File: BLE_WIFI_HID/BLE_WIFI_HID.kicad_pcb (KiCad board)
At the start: 2 copper layers, 63.3 x 34 mm, 22 parts, among them P1 CONN_01X07, P2 CONN_01X07, P3 PROGRAMMER SERIAL, P4 Battery, SW1 SW_Push, U1 ESP32-WROOM, U2 AP2112K-3.3TRG1, U3 MCP73831T-2ACI/OT

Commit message: clean and new position
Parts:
- moved R6 5.18 mm to (178.0, 85.0)
- moved C4 4.67 mm to (184.2, 91.3)
- moved U3 4.04 mm to (178.2, 90.0)
- moved P4 3.88 mm to (183.0, 85.9)
- moved R3 3.80 mm to (152.8, 84.9), turned to 90 degrees
- moved P3 3.76 mm to (136.5, 84.4)
- moved C3 2.31 mm to (174.1, 99.9)
- moved D2 2.24 mm to (177.6, 99.8)
- moved SW1 2.00 mm to (168.5, 102.0)
- moved D1 1.88 mm to (156.8, 83.5)
- moved R7 1.86 mm to (169.9, 88.3)
- moved C2 1.74 mm to (181.7, 104.9)
- moved D3 1.65 mm to (173.2, 88.3)
- moved U2 1.40 mm to (182.2, 100.4)
- moved R5 1.13 mm to (181.6, 107.8)
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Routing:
- net VCC: track 126.3 -> 183.3 mm
- net GND: track 176.0 -> 197.0 mm
- net /IO0_BOOT/DTR: track 25.5 -> 15.9 mm
- net /TX_ESP32: track 42.6 -> 33.0 mm
- net /IO13: track 13.1 -> 6.50 mm
- net /RX_ESP32: track 36.2 -> 30.9 mm
- net +3V3: track 35.6 -> 30.3 mm
- net Net-(R7-Pad1): track 12.6 -> 7.97 mm
- net Net-(R7-Pad2): track 9.25 -> 13.3 mm
- net /RESET/RTS: track 56.1 -> 52.1 mm
- net Net-(D3-Pad1): track 2.14 -> 5.33 mm
- net Net-(D3-Pad2): track 2.83 -> 5.06 mm
- net +BATT: track 30.2 -> 28.4 mm
- added copper zone on F.Cu, net GND
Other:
- board size 63.3 x 34 mm -> 62.9 x 33.4 mm

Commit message: change the connectors
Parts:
- P1, P2: moved to B.Cu
- turned P1 to 0 degrees
- turned P2 to 180 degrees

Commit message: Auto stash before merge of "master" and "origin/master"
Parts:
- moved C3 68.7 mm to (120.5, 56.9)
- moved C1 68.7 mm to (115.1, 63.0)
- moved C2 68.7 mm to (128.1, 61.9)
- moved C4 68.7 mm to (130.6, 48.4)
- moved D1 68.7 mm to (103.2, 40.5)
- moved D2 68.7 mm to (124.0, 56.8)
- moved D3 68.7 mm to (119.7, 45.4)
- moved P3 68.7 mm to (82.9, 41.4)
- moved P4 68.7 mm to (129.4, 42.9)
- moved R1 68.7 mm to (116.2, 50.9)
- moved R2 68.7 mm to (113.6, 50.9)
- moved R3 68.7 mm to (99.3, 41.9)
- moved R4 68.7 mm to (114.6, 55.6)
- moved R5 68.7 mm to (128.1, 64.8)
- moved R6 68.7 mm to (124.4, 42.0)
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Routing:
- net GND: track 197.0 -> 202.6 mm
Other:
- outline, holes or cut-outs redrawn

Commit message: update to v0.3 pcb
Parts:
- removed P1, P2: CONN_01X07, Pin_Headers:Pin_Header_Straight_1x07_Pitch2.54mm
- removed SW1: SW_Push, TIH:SW_B3U-1000P
- added G***: LOGO, Aesthetics:electronic_cats_logo_8x6, B.Cu at (111.7, 49.4)
- added G***: LOGO, Aesthetics:meowmeow_logo_21x8, B.Cu at (113.5, 38.9)
- added G***: LOGO, Aesthetics:beta_testing, F.Cu at (83.4, 64.2)
- added J1: Conn_02x03_Odd_Even, Pines:62000621121, F.Cu at (136.4, 53.7)
- added J2: Conn_02x03_Odd_Even, Pines:62000621121, F.Cu at (80.8, 53.5)
- added R8: 10K, Resistors_SMD:R_0805_HandSoldering, F.Cu at (120.0, 65.3)
- R4: value 1k -> 10k
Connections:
- net /IO0_BOOT/DTR renamed /ESP_GPIO0
- net /RX_ESP32 renamed /ESP_RX
- net /TX_ESP32 renamed /ESP_TX
- P3 pad 5: /RESET/RTS -> /ESP_RESET
- R3 pad 1: /IO13 -> /IO25
- R4 pad 1: +3V3 -> /ESP_RESET
- R4 pad 2: /RESET/RTS -> GND
- U1 pad 10: Net-(U1-Pad10) -> /IO25
- U1 pad 13: Net-(U1-Pad13) -> /MOSI
- U1 pad 16: /IO13 -> Net-(U1-Pad16)
- U1 pad 29: Net-(U1-Pad29) -> /ESP_CS
- U1 pad 3: /RESET/RTS -> /ESP_RESET
- U1 pad 30: Net-(U1-Pad30) -> /SCK
- U1 pad 31: Net-(U1-Pad31) -> /ESP_RTS
- U1 pad 37: Net-(U1-Pad37) -> /MISO
- U1 pad 7: /AN35_BAT -> Net-(U1-Pad7)
- U1 pad 9: Net-(U1-Pad9) -> /ESP_BUSY
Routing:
- net GND: track 202.6 -> 0.00 mm
- net VCC: track 183.4 -> 0.00 mm
- net /RESET/RTS: track 52.1 -> 0.00 mm
- net /ESP_TX: track 32.9 -> 0.00 mm
- net /ESP_RX: track 30.9 -> 0.00 mm
- net +3V3: track 30.3 -> 0.00 mm
- net +BATT: track 28.4 -> 0.00 mm
- net /ESP_GPIO0: track 15.9 -> 0.00 mm
- net /AN35_BAT: track 14.3 -> 0.00 mm
- net Net-(R7-Pad2): track 13.3 -> 0.00 mm
- net Net-(R7-Pad1): track 7.97 -> 0.00 mm
- net Net-(R5-Pad1): track 7.97 -> 0.00 mm
- net /IO13: track 6.50 -> 0.00 mm
- net Net-(D3-Pad1): track 5.33 -> 0.00 mm
- net Net-(D3-Pad2): track 5.06 -> 0.00 mm
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
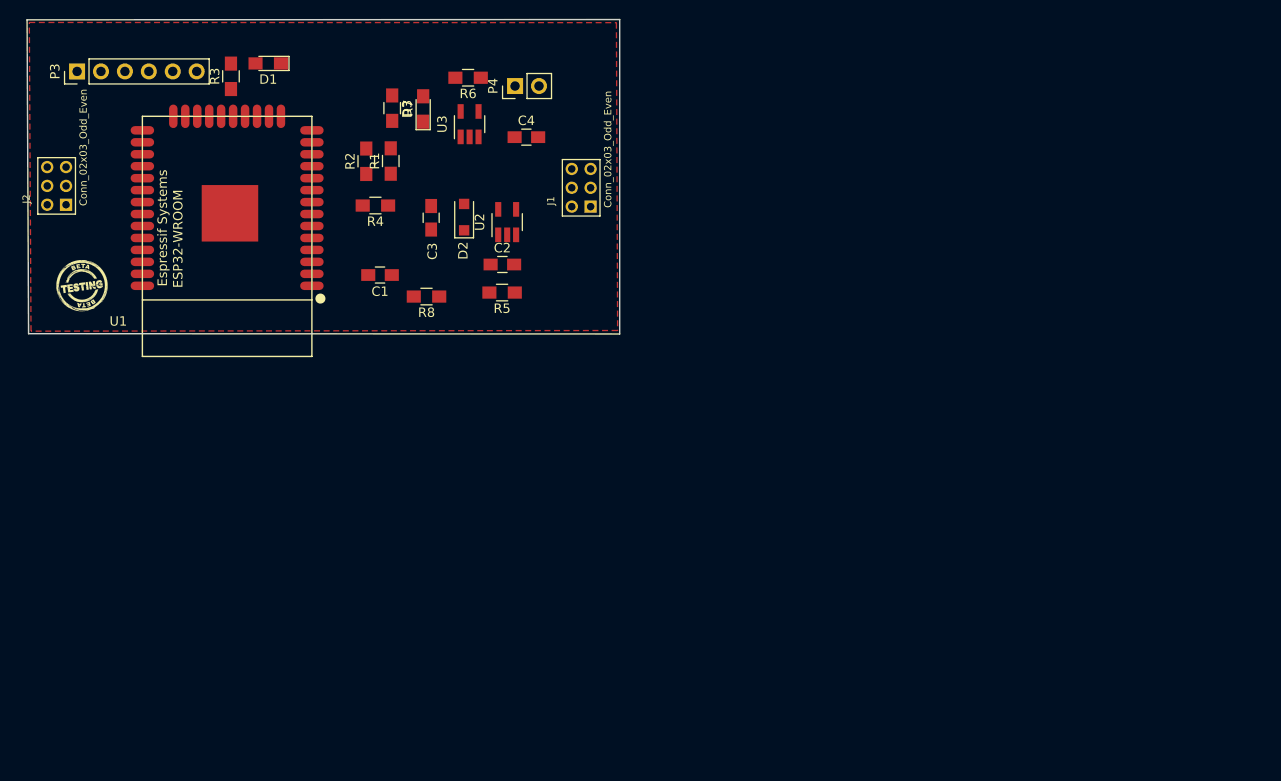
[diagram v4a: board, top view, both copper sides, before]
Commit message: update reset resistor ESP32
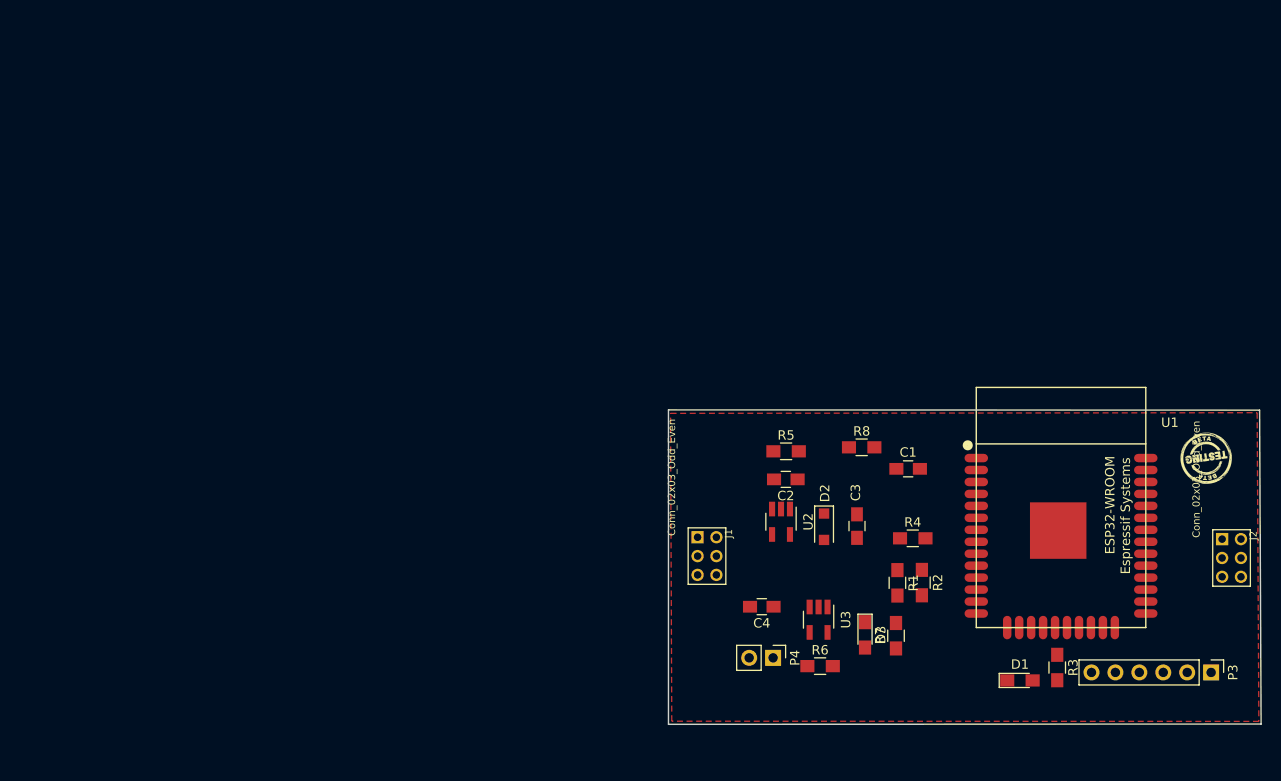
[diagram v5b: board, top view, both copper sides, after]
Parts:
- moved P3 136.3 mm to (203.3, 105.2), turned to 270 degrees
- moved J2 130.9 mm to (205.5, 93.0), turned to 270 degrees
- moved G*** 120.8 mm to (202.8, 82.3), turned to 180 degrees
- moved R3 107.9 mm to (187.0, 104.7), turned to 270 degrees
- moved D1 103.3 mm to (183.0, 106.0), turned to 0 degrees
- moved U1 93.1 mm to (187.4, 87.7), turned to 180 degrees
- moved G*** 92.9 mm to (195.7, 89.0)
- moved G*** 92.1 mm to (195.7, 80.4)
- moved R7 77.5 mm to (169.9, 101.3), turned to 90 degrees
- moved R2 74.0 mm to (172.6, 95.6), turned to 270 degrees
- moved D3 72.9 mm to (166.6, 101.2), turned to 270 degrees
- moved R6 72.8 mm to (161.8, 104.5), turned to 0 degrees
- moved R1 70.0 mm to (170.0, 95.7), turned to 270 degrees
- moved R4 67.1 mm to (171.7, 90.9), turned to 0 degrees
- moved P4 66.6 mm to (156.8, 103.6), turned to 270 degrees
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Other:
- outline, holes or cut-outs redrawn
- board text added: "Backpack BLE"

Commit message: Inicio routeo
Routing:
- net /ESP_GPIO0: track 0.00 -> 89.1 mm
- net /MOSI: track 0.00 -> 61.6 mm
- net /ESP_CS: track 0.00 -> 51.7 mm
- net +BATT: track 0.00 -> 25.8 mm
- net Net-(R7-Pad1): track 0.00 -> 13.4 mm
- net /ESP_RESET: track 0.00 -> 13.1 mm
- net Net-(R7-Pad2): track 0.00 -> 11.9 mm
- net +3V3: track 0.00 -> 11.5 mm
- net Net-(D3-Pad2): track 0.00 -> 5.18 mm
- net /AN35_BAT: track 0.00 -> 5.03 mm
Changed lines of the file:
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@@
-(kicad_pcb (version 20171130) (host pcbnew "(5.0.1-3-g963ef8bb5)")
+(kicad_pcb (version 20171130) (host pcbnew "(5.1.2)-2")
   (general
     (thickness 1.6)
     (drawings 5)
-    (tracks 1)
+    (tracks 83)
     (zones 0)
     (modules 25)
@@
     (zone_45_only no)
     (trace_min 0.2)
-    (segment_width 0.2)
-    (edge_width 0.15)
     (via_size 0.6)
     (via_drill 0.4)
@@
     (uvia_min_size 0.2)
     (uvia_min_drill 0.1)
+    (edge_width 0.15)
+    (segment_width 0.2)
     (pcb_text_width 0.3)
     (pcb_text_size 1.5 1.5)
@@
   (gr_line (start 208.648 110.668) (end 145.718 110.698) (layer Edge.Cuts) (width 0.15))
   (gr_line (start 208.488 77.338) (end 208.648 110.668) (layer Edge.Cuts) (width 0.15))
+  (segment (start 175.6 85.45) (end 170.2 85.45) (width 0.3) (layer F.Cu) (net 1))
+  (segment (start 169.918 85.168) (end 169.918 83.568) (width 0.3) (layer F.Cu) (net 1))
+  (segment (start 170.2 85.45) (end 169.918 85.168) (width 0.3) (layer F.Cu) (net 1))
+  (segment (start 175.95 84.075) (end 175.95 85.1) (width 0.3) (layer F.Cu) (net 1))
+  (segment (start 176.332 83.693) (end 175.95 84.075) (width 0.3) (layer F.Cu) (net 1))
+  (segment (start 178.403 83.693) (end 176.332 83.693) (width 0.3) (layer F.Cu) (net 1))
+  (segment (start 175.95 85.1) (end 175.6 85.45) (width 0.3) (layer F.Cu) (net 1))
+  (segment (start 160.678 98.208) (end 160.708 98.238) (width 0.3) (layer F.Cu) (net 4))
+  (segment (start 156.878 98.208) (end 160.678 98.208) (width 0.3) (layer F.Cu) (net 4))
+  (segment (start 156.828 98.258) (end 156.878 98.208) (width 0.3) (layer F.Cu) (net 4))
+  (segment (start 156.828 103.638) (end 156.828 98.258) (width 0.3) (layer F.Cu) (net 4))
+  (segment (start 162.238 94.038) (end 162.238 91.118) (width 0.3) (layer F.Cu) (net 4))
+  (segment (start 160.708 98.238) (end 160.708 95.917) (width 0.3) (layer F.Cu) (net 4))
+  (segment (start 162.523 94.323) (end 162.4125 94.2125) (width 0.3) (layer F.Cu) (net 4))
+  (segment (start 162.4125 94.2125) (end 162.238 94.038) (width 0.3) (layer F.Cu) (net 4))
+  (segment (start 162.2375 94.0385) (end 162.238 94.038) (width 0.3) (layer F.Cu) (net 4))
+  (segment (start 162.2375 94.3875) (end 162.2375 94.0385) (width 0.3) (layer F.Cu) (net 4))
+  (segment (start 162.2375 94.3875) (end 162.4125 94.2125) (width 0.3) (layer F.Cu) (net 4))
+  (segment (start 162.302 94.323) (end 162.15 94.475) (width 0.3) (layer F.Cu) (net 4))
+  (segment (start 162.727 94.323) (end 162.302 94.323) (width 0.3) (layer F.Cu) (net 4))
+  (segment (start 162.15 94.475) (end 162.2375 94.3875) (width 0.3) (layer F.Cu) (net 4))
+  (segment (start 160.708 95.917) (end 162.15 94.475) (width 0.3) (layer F.Cu) (net 4))
+  (segment (start 170.028 94.323) (end 162.727 94.323) (width 0.3) (layer F.Cu) (net 4))
+  (segment (start 162.727 94.323) (end 162.523 94.323) (width 0.3) (layer F.Cu) (net 4))
   (segment (start 184.408 106.018) (end 184.388 106.038) (width 0.3) (layer F.Cu) (net 5))
+  (segment (start 163.168 104.518) (end 166.232 104.518) (width 0.3) (layer F.Cu) (net 7))
+  (segment (start 166.588 104.162) (end 166.588 102.548) (width 0.3) (layer F.Cu) (net 7))
+  (segment (start 166.232 104.518) (end 166.588 104.162) (width 0.3) (layer F.Cu) (net 7))
+  (segment (start 178.403 97.663) (end 176.162 97.663) (width 0.3) (layer F.Cu) (net 8))
+  (segment (start 176.162 97.663) (end 175.2 98.625) (width 0.3) (layer F.Cu) (net 8))
+  (segment (start 175.2 98.625) (end 175.2 107.9) (width 0.3) (layer F.Cu) (net 8))
+  (segment (start 175.2 107.9) (end 174.675 108.425) (width 0.3) (layer F.Cu) (net 8))
+  (segment (start 174.675 108.425) (end 153.225 108.425) (width 0.3) (layer F.Cu) (net 8))
+  (segment (start 153.225 108.425) (end 152.525 107.725) (width 0.3) (layer F.Cu) (net 8))
+  (segment (start 152.525 107.725) (end 152.525 88.925) (width 0.3) (layer F.Cu) (net 8))
+  (segment (start 152.525 88.925) (end 151.625 88.025) (width 0.3) (layer F.Cu) (net 8))
+  (segment (start 151.625 88.025) (end 149.025 88.025) (width 0.3) (layer F.Cu) (net 8))
+  (segment (start 148.808 88.242) (end 148.808 90.833) (width 0.3) (layer F.Cu) (net 8))
+  (segment (start 149.025 88.025) (end 148.808 88.242) (width 0.3) (layer F.Cu) (net 8))
+  (segment (start 171.678 94.298) (end 171.4 94.576) (width 0.3) (layer F.Cu) (net 11))
+  (segment (start 172.628 94.298) (end 171.678 94.298) (width 0.3) (layer F.Cu) (net 11))
+  (segment (start 171.4 94.576) (end 171.4 96.8) (width 0.3) (layer F.Cu) (net 11))
+  (segment (start 171.177 97.023) (end 170.028 97.023) (width 0.3) (layer F.Cu) (net 11))
+  (segment (start 171.4 96.8) (end 171.177 97.023) (width 0.3) (layer F.Cu) (net 11))
+  (segment (start 168.928 102.638) (end 168 101.71) (width 0.3) (layer F.Cu) (net 13))
+  (segment (start 169.878 102.638) (end 168.928 102.638) (width 0.3) (layer F.Cu) (net 13))
+  (segment (start 168 101.71) (end 168 98.575) (width 0.3) (layer F.Cu) (net 13))
+  (segment (start 168 98.575) (end 167.425 98) (width 0.3) (layer F.Cu) (net 13))
+  (segment (start 167.425 98) (end 165.25 98) (width 0.3) (layer F.Cu) (net 13))
+  (segment (start 165.25 98) (end 164.55 98.7) (width 0.3) (layer F.Cu) (net 13))
+  (segment (start 164.55 98.7) (end 164.55 100.75) (width 0.3) (layer F.Cu) (net 13))
+  (segment (start 164.362 100.938) (end 162.608 100.938) (width 0.3) (layer F.Cu) (net 13))
+  (segment (start 164.55 100.75) (end 164.362 100.938) (width 0.3) (layer F.Cu) (net 13))
+  (segment (start 168.928 99.938) (end 168.525 99.535) (width 0.3) (layer F.Cu) (net 14))
+  (segment (start 169.878 99.938) (end 168.928 99.938) (width 0.3) (layer F.Cu) (net 14))
+  (segment (start 168.525 99.535) (end 168.525 98.05) (width 0.3) (layer F.Cu) (net 14))
+  (segment (start 168.525 98.05) (end 167.075 96.6) (width 0.3) (layer F.Cu) (net 14))
+  (segment (start 167.075 96.6) (end 162 96.6) (width 0.3) (layer F.Cu) (net 14))
+  (segment (start 161.658 96.942) (end 161.658 98.238) (width 0.3) (layer F.Cu) (net 14))
+  (segment (start 162 96.6) (end 161.658 96.942) (width 0.3) (layer F.Cu) (net 14))
+  (segment (start 196.403 98.933) (end 203.033 98.933) (width 0.3) (layer F.Cu) (net 36))
+  (segment (start 203.338 99.238) (end 203.338 105.188) (width 0.3) (layer F.Cu) (net 36))
+  (segment (start 203.033 98.933) (end 203.338 99.238) (width 0.3) (layer F.Cu) (net 36))
+  (segment (start 196.403 98.933) (end 197.203 98.933) (width 0.3) (layer F.Cu) (net 36))
+  (segment (start 150.808 106.715122) (end 150.808 94.833) (width 0.3) (layer F.Cu) (net 36))
+  (segment (start 206.163 105.188) (end 206.625 105.65) (width 0.3) (layer F.Cu) (net 36))
+  (segment (start 203.338 105.188) (end 206.163 105.188) (width 0.3) (layer F.Cu) (net 36))
+  (segment (start 206.625 105.65) (end 206.625 108.575) (width 0.3) (layer F.Cu) (net 36))
+  (segment (start 206.625 108.575) (end 206.125 109.075) (width 0.3) (layer F.Cu) (net 36))
+  (segment (start 206.125 109.075) (end 153.167878 109.075) (width 0.3) (layer F.Cu) (net 36))
+  (segment (start 153.167878 109.075) (end 150.808 106.715122) (width 0.3) (layer F.Cu) (net 36))
+  (segment (start 176.853 84.963) (end 175.691 86.125) (width 0.3) (layer F.Cu) (net 37))
+  (segment (start 178.403 84.963) (end 176.853 84.963) (width 0.3) (layer F.Cu) (net 37))
+  (segment (start 175.691 86.125) (end 170.825 86.125) (width 0.3) (layer F.Cu) (net 37))
+  (segment (start 170.308 86.642) (end 170.308 90.948) (width 0.3) (layer F.Cu) (net 37))
+  (segment (start 170.825 86.125) (end 170.308 86.642) (width 0.3) (layer F.Cu) (net 37))
+  (segment (start 196.403 93.853) (end 200.197 93.853) (width 0.3) (layer F.Cu) (net 42))
+  (segment (start 200.197 93.853) (end 201.35 92.7) (width 0.3) (layer F.Cu) (net 42))
+  (segment (start 201.35 92.7) (end 201.35 80.875) (width 0.3) (layer F.Cu) (net 42))
+  (segment (start 200.757999 80.282999) (end 171.992001 80.282999) (width 0.3) (layer F.Cu) (net 42))
+  (segment (start 201.35 80.875) (end 200.757999 80.282999) (width 0.3) (layer F.Cu) (net 42))
+  (segment (start 170.992 81.283) (end 167.583 81.283) (width 0.3) (layer F.Cu) (net 42))
+  (segment (start 171.992001 80.282999) (end 170.992 81.283) (width 0.3) (layer F.Cu) (net 42))
   (zone (net 2) (net_name GND) (layer F.Cu) (hatch edge 0.508)
     (connect_pads (clearance 0.508))
     (min_thickness 0.254)
-    (fill yes (arc_segments 16) (thermal_gap 0.508) (thermal_bridge_width 0.508))
+    (fill (arc_segments 16) (thermal_gap 0.508) (thermal_bridge_width 0.508))
     (polygon
       (pts
